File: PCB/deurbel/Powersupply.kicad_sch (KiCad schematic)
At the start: 6 parts, among them J4 Powerline, U2 LM7805_TO220

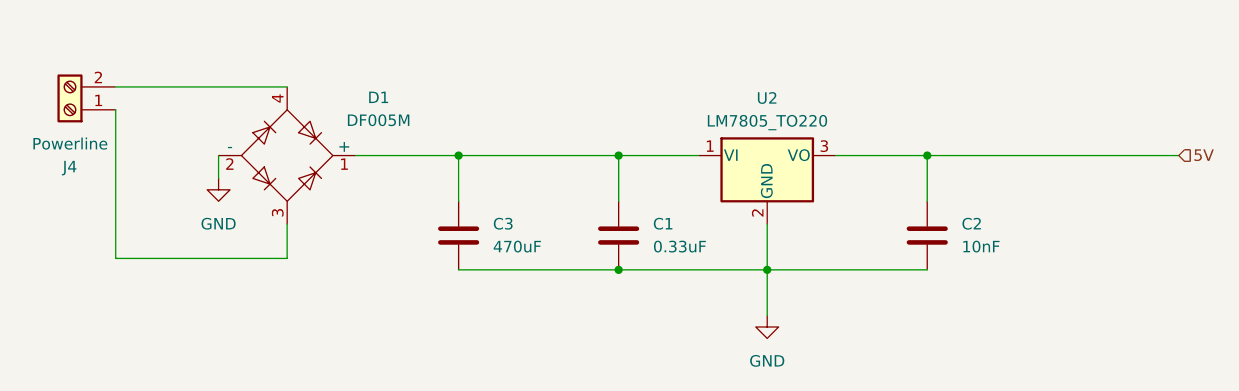
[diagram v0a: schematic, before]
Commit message: Client config is now done once and removed scanning from connection task
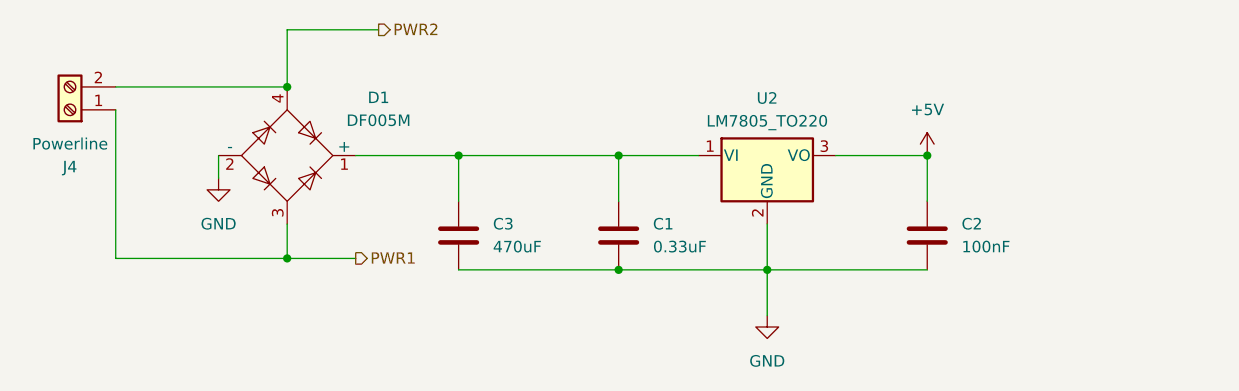
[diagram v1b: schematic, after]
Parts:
- C2: value 10nF -> 100nF
- C3: footprint Capacitor_THT:C_Disc_D4.3mm_W1.9mm_P5.00mm -> Capacitor_THT:CP_Radial_D10.0mm_P5.00mm
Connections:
- net PWR1: now reaches D1.3, J4.1 (Pin_1)
- net PWR2: now reaches D1.4, J4.2 (Pin_2)
- net 5V renamed +5V
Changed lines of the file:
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@@
+	)
+	(junction
+		(at 49.53 111.76)
+		(diameter 0)
+		(color 0 0 0 0)
 	)
 	(junction
@@
 	)
 	(junction
+		(at 49.53 92.71)
+		(diameter 0)
+		(color 0 0 0 0)
+	)
+	(junction
 		(at 86.36 100.33)
 		(diameter 0)
@@
 	(wire
 		(pts
-			(xy 120.65 100.33) (xy 148.59 100.33)
-		)
-		(stroke
-			(width 0)
-			(type default)
-		)
-	)
-	(wire
-		(pts
 			(xy 49.53 111.76) (xy 30.48 111.76)
 		)
@@
 	(wire
 		(pts
+			(xy 49.53 111.76) (xy 57.15 111.76)
+		)
+		(stroke
+			(width 0)
+			(type default)
+		)
+	)
+	(wire
+		(pts
 			(xy 86.36 100.33) (xy 95.25 100.33)
 		)
@@
 	(wire
 		(pts
+			(xy 49.53 86.36) (xy 49.53 92.71)
+		)
+		(stroke
+			(width 0)
+			(type default)
+		)
+	)
+	(wire
+		(pts
+			(xy 59.69 86.36) (xy 49.53 86.36)
+		)
+		(stroke
+			(width 0)
+			(type default)
+		)
+	)
+	(wire
+		(pts
 			(xy 102.87 113.03) (xy 102.87 107.95)
 		)
@@
 		)
 	)
-	(hierarchical_label "5V"
-		(shape input)
-		(at 148.59 100.33 0)
+	(hierarchical_label "PWR2"
+		(shape output)
+		(at 59.69 86.36 0)
+		(effects
+			(font
+				(size 1.27 1.27)
+			)
+			(justify left)
+		)
+	)
+	(hierarchical_label "PWR1"
+		(shape output)
+		(at 57.15 111.76 0)
 		(effects
 			(font
@@
 	)
 	(symbol
+		(lib_id "power:+5V")
+		(at 120.65 100.33 0)
+		(unit 1)
+		(exclude_from_sim no)
+		(in_bom yes)
+		(on_board yes)
+		(dnp no)
+		(fields_autoplaced yes)
+		(property "Reference" "#PWR013"
+			(at 120.65 104.14 0)
+			(effects
+				(font
+					(size 1.27 1.27)
+				)
+				(hide yes)
+			)
+		)
+		(property "Value" "+5V"
+			(at 120.65 95.25 0)
+			(effects
+				(font
+					(size 1.27 1.27)
+				)
+			)
+		)
+		(property "Footprint" ""
+			(at 120.65 100.33 0)
+			(effects
+				(font
+					(size 1.27 1.27)
+				)
+				(hide yes)
+			)
+		)
+		(property "Datasheet" ""
+			(at 120.65 100.33 0)
+			(effects
+				(font
+					(size 1.27 1.27)
+				)
+				(hide yes)
+			)
+		)
+		(property "Description" "Power symbol creates a global label with name \"+5V\""
+			(at 120.65 100.33 0)
+			(effects
+				(font
+					(size 1.27 1.27)
+				)
+				(hide yes)
+			)
+		)
+		(pin "1"
+		)
+		(instances
+			(project ""
+				(path "/67131908-ece0-40ca-a97d-910c6fc709a1/97c7c8ea-88a4-47d1-b5a2-7be5d0905397"
+					(reference "#PWR013")
+					(unit 1)
+				)
+			)
+		)
+	)
+	(symbol
 		(lib_id "Device:C")
 		(at 68.58 109.22 0)
@@
 			)
 		)
-		(property "Footprint" "Capacitor_THT:C_Disc_D4.3mm_W1.9mm_P5.00mm"
+		(property "Footprint" "Capacitor_THT:CP_Radial_D10.0mm_P5.00mm"
 			(at 69.5452 113.03 0)
 			(effects
@@
 			)
 		)
-		(property "Value" "10nF"
+		(property "Value" "100nF"
 			(at 124.46 110.4899 0)
 			(effects
